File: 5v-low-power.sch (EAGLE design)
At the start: 34 parts, among them J1 Bypass, J2 En, J3 12v, J4 5V Out, J5 LED EN, J6 POWERPOLE_POWER25A, J7 POWERPOLE_POWER25A, Q1 SI4532ADY, U1 LT1934ES6TRMPBF

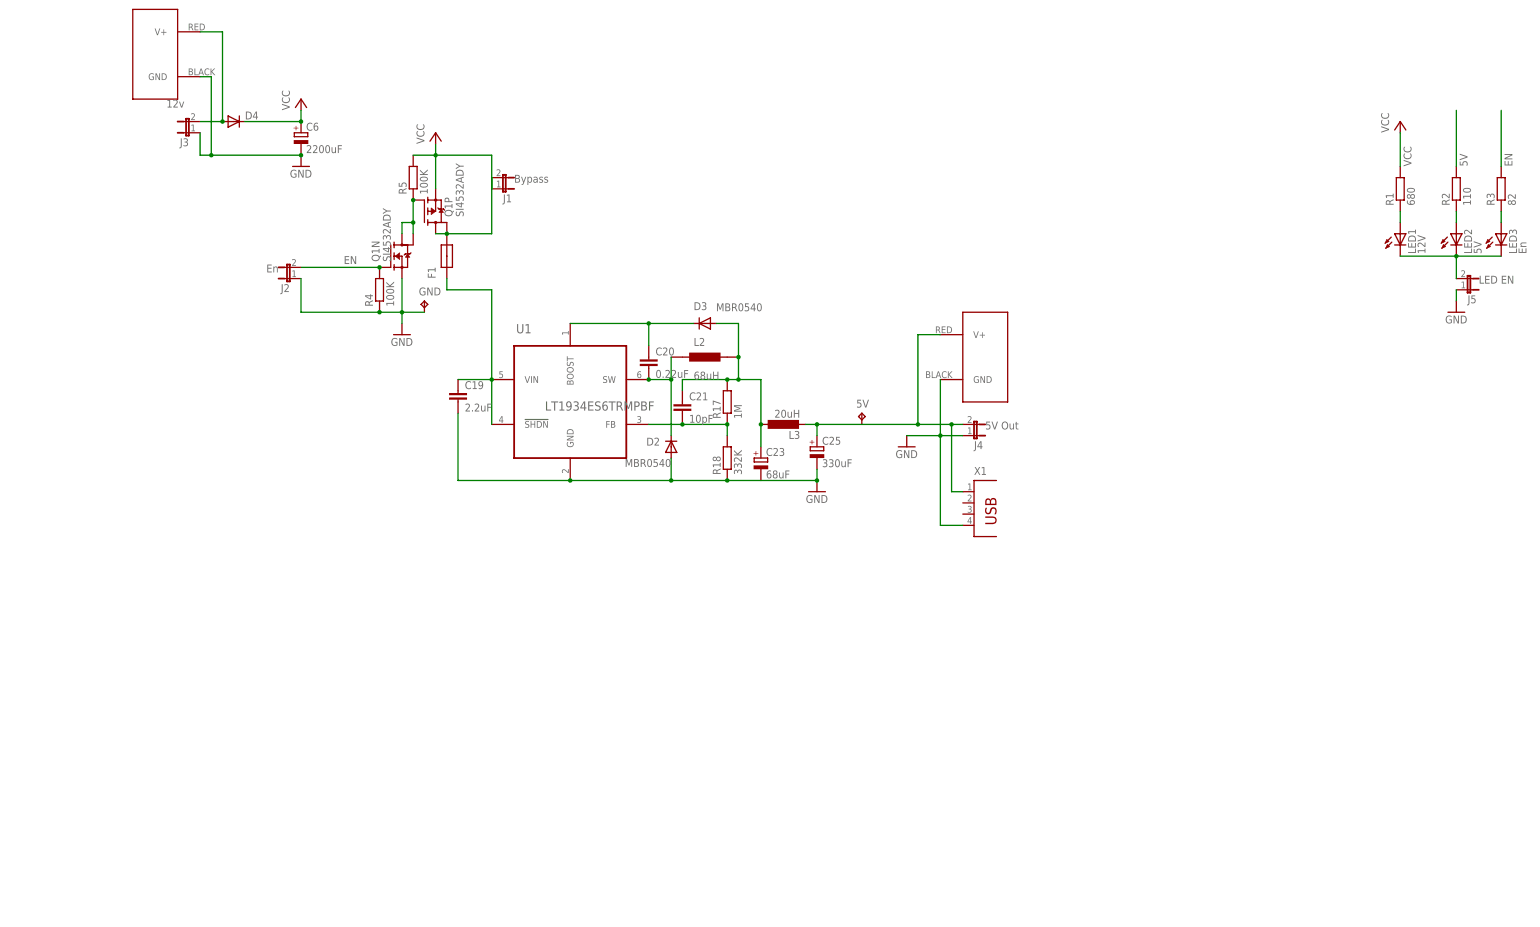
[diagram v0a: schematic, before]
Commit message: uses a4 frame and smaller ground plane area to make printing better
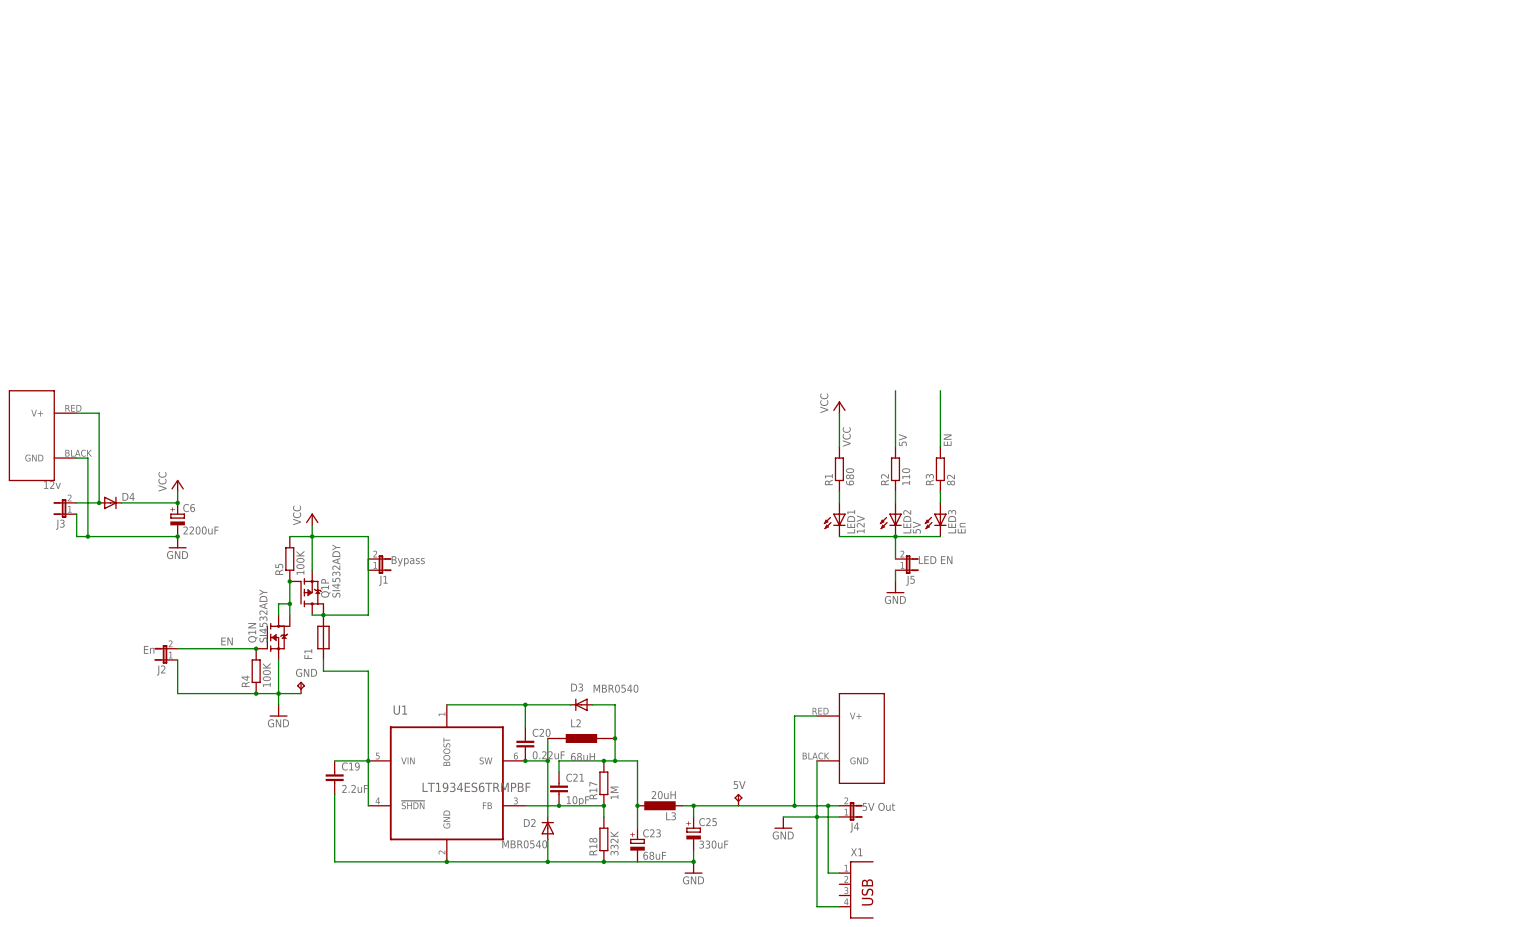
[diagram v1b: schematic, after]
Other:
- note removed: "PSU"
- moved on the sheet: 5V, C19, C20, C21, C23, C25, C6, D2, D3, D4, F1, GND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
